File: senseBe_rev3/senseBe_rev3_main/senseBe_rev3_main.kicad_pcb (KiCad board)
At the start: 2 copper layers, 40 x 45 mm, 48 parts, among them P1 CONN_02X05, Q1 SI2302, Q2 SI2302, Q3 SI2302, Q4 SI2302, Q5 SI2302, Q6 SI2302, U1 MDBT42Q, U2 TSSP4056, U3 AP3405, Y1 MC-146_32.768KA-AC3_ROHS

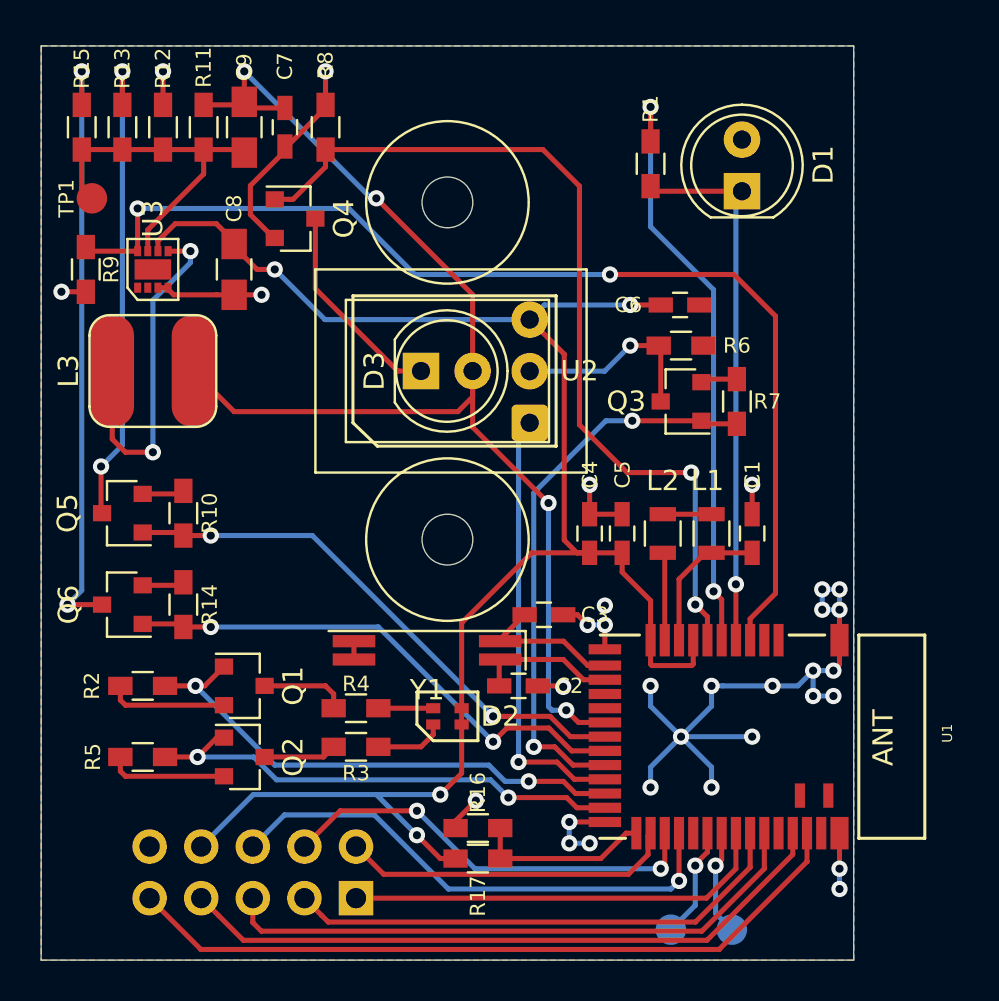
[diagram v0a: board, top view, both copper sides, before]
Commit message: Add marking for Tx and Rx regions, add Appiko Logo and revision name
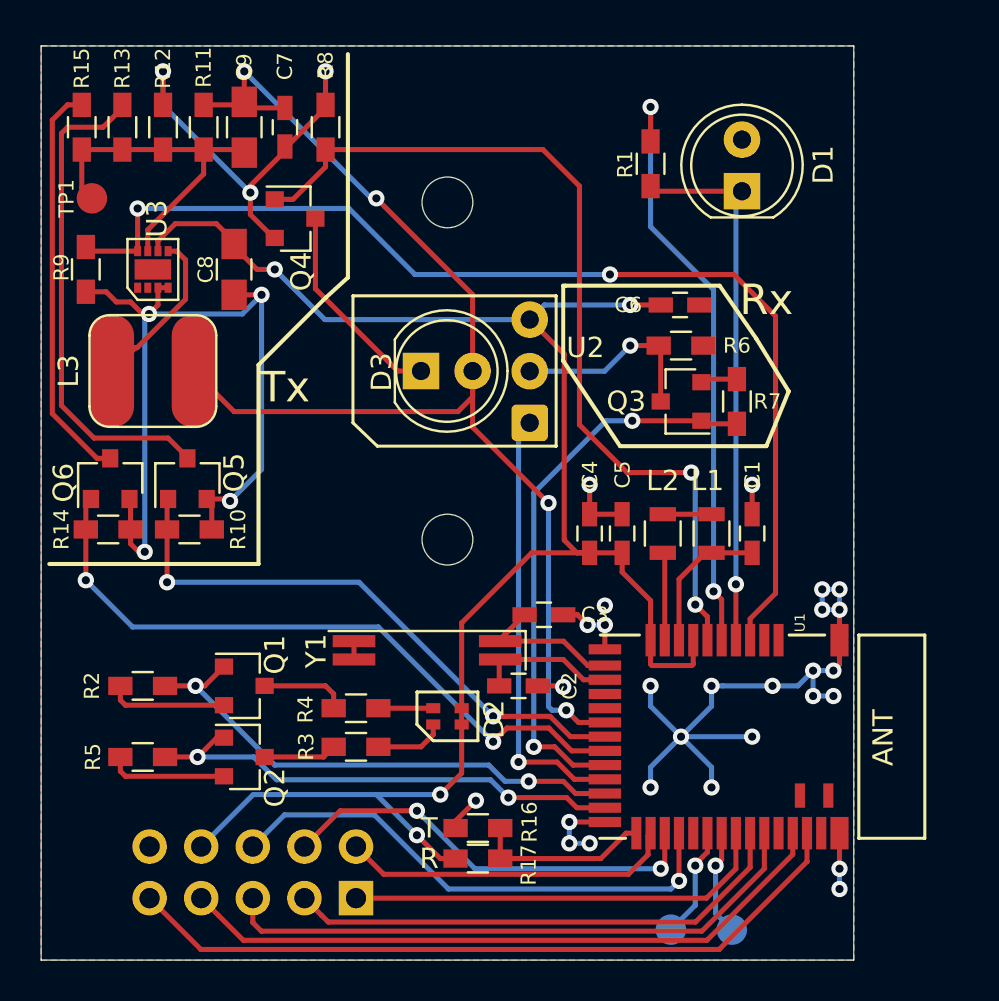
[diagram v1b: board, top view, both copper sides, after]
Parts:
- added G***: LOGO, Appiko_Logo:Appiko_logo4, B.Cu at (37.4, 48.9)
- moved Q6 6.23 mm to (13.4, 31.3), turned to 90 degrees
- moved R14 5.23 mm to (13.3, 33.8), turned to 0 degrees
- moved Q5 3.62 mm to (17.2, 31.3), turned to 90 degrees
- moved R10 0.85 mm to (17.3, 33.8), turned to 0 degrees
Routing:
- net GND: track 85.1 -> 123.6 mm, vias 31 -> 34
- net Net-(Q6-Pad3): track 29.9 -> 20.0 mm, vias 2 -> 0
- net Net-(L3-Pad1): track 17.4 -> 8.05 mm, vias 2 -> 0
- net /PWR2: track 25.9 -> 33.7 mm
- net /PWR1: track 26.9 -> 28.8 mm
- net Net-(Q5-Pad3): track 23.9 -> 24.4 mm, vias 2 -> 0
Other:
- board text added: "R"
- board text added: "Rx"
- board text added: "SenseBe rev3"
- board text added: "T"
- board text added: "Tx"

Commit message: Added OSHW logo and moved Appiko Logo
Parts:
- added G***: LOGO, Appiko_Logo:OSHW1, B.Cu at (20.8, 23.4)
- moved G*** 2.56 mm to (39.0, 46.9)
